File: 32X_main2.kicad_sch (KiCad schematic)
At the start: 43 parts, among them IC10 TC511664, IC509 74AC04, IC510 RHSRL33A, IC7 315-5818-B, IC8 315-5781, IC9 TC511664

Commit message: Start PCB layout.
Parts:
- removed IC7: 315-5818-B, symbol 32X:315-5818-B
- added IC504: 315-5818, Package_QFP:LQFP-176_24x24mm_P0.5mm, symbol 32X:315-5818
- C511, C512, C513, C514, C515, C516, C520, C521, C522, C523, C525, C526, C530, C531, C532, C533, C534, C535, C537, C538, C539, C540, C541, C596, C597, C599: footprint (none) -> Capacitor_SMD:C_0805_2012Metric
- IC501, IC502: value ~ -> SH2; footprint (none) -> Package_QFP:LQFP-144_20x20mm_P0.5mm
- IC503: value ~ -> uPD4502161; footprint (none) -> Package_SO:TSSOP-50_4.4x12.5mm_P0.5mm
- IC506: renamed from IC8; footprint (none) -> Package_QFP:LQFP-144_20x20mm_P0.5mm
- IC507: renamed from IC9; footprint (none) -> Package_SO:VSO-40_7.6x15.4mm_P0.762mm
- IC508: renamed from IC10; footprint (none) -> Package_SO:VSO-40_7.6x15.4mm_P0.762mm
- IC509: footprint (none) -> Package_SO:SO-14_3.9x8.65mm_P1.27mm
- R502, R503, R505, R506, R507, R508, R509: footprint (none) -> Resistor_SMD:R_0805_2012Metric
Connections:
- net GND: now also IC504.111 (GND), IC504.133 (GND), IC504.134 (GND), IC504.175 (GND), IC504.176 (GND), IC504.23 (GND), IC504.45 (GND), IC504.46 (GND), IC504.87 (GND), IC504.88 (GND)
- net SHA1: now also IC504.35 (SHA1)
- net SHA10: now also IC504.47 (SHA10)
- net SHA11: now also IC504.48 (SHA11)
- net SHA12: now also IC504.49 (SHA12)
- net SHA13: now also IC504.50 (SHA13)
- net SHA14: now also IC504.51 (SHA14)
- net SHA15: now also IC504.52 (SHA15)
- net SHA16: now also IC504.53 (SHA16)
- net SHA17: now also IC504.54 (SHA17)
- net SHA2: now also IC504.36 (SHA2)
- net SHA3: now also IC504.37 (SHA3)
- net SHA4: now also IC504.38 (SHA4)
- net SHA5: now also IC504.39 (SHA5)
- net SHA6: now also IC504.40 (SHA6)
- net SHA7: now also IC504.41 (SHA7)
- net SHA8: now also IC504.42 (SHA8)
- net SHA9: now also IC504.43 (SHA9)
- net SHD0: now also IC504.26 (SHD0)
- net SHD1: now also IC504.25 (SHD1)
- net SHD10: now also IC504.14 (SHD10)
- net SHD11: now also IC504.13 (SHD11)
- net SHD12: now also IC504.12 (SHD12)
- net SHD13: now also IC504.11 (SHD13)
- net SHD14: now also IC504.10 (SHD14)
- net SHD15: now also IC504.9 (SHD15)
- net SHD2: now also IC504.24 (SHD2)
- net SHD3: now also IC504.21 (SHD3)
- net SHD4: now also IC504.20 (SHD4)
- net SHD5: now also IC504.19 (SHD5)
- net SHD6: now also IC504.18 (SHD6)
- net SHD7: now also IC504.17 (SHD7)
- net SHD8: now also IC504.16 (SHD8)
- net SHD9: now also IC504.15 (SHD9)
- net SHDREQ0: now also IC504.66 (~{DREQ0})
- net SHDREQ1: now also IC504.65 (~{DREQ1})
- net SHRDWR: now also IC504.59 (RDWR)
- net VCC2: now also IC504.1 (VCC), IC504.110 (VCC), IC504.132 (VCC), IC504.22 (VCC), IC504.44 (VCC), IC504.89 (VCC)
- net ~{SHBS}: now also IC504.60 (~{BS})
- net ~{SHCS0M}: now also IC504.64 (~{CS0M})
- net ~{SHCS0S}: now also IC504.63 (~{CS0S})
- net ~{SHCS1}: now also IC504.62 (~{CS1})
- net ~{SHCS2}: now also IC504.61 (~{CS2})
- net ~{SHDQMLL}: now also IC504.57 (~{DQLL})
- net ~{SHDQMLU}: now also IC504.58 (~{DQLU})
- net ~{SHMIRL1}: now also IC504.30 (~{MIRL1})
- net ~{SHMIRL2}: now also IC504.31 (~{MIRL2})
- net ~{SHMIRL3}: now also IC504.32 (~{MIRL3})
- net ~{SHRD0}: now also IC504.56 (~{RD})
- net ~{SHRES}: now also IC504.34 (~{SHRES})
- net ~{SHSIRL1}: now also IC504.27 (~{SIRL1})
- net ~{SHSIRL2}: now also IC504.28 (~{SIRL2})
- net ~{SHSIRL3}: now also IC504.29 (~{SIRL3})
- net ~{SHWAIT}: now also IC504.55 (~{WAIT})
- net at C525.1, IC506.61 (ACCS): now also IC504.125 (ACCS)
- net at IC506.39 (AD15): now also IC504.150 (AD15)
- net at IC506.40 (AD14): now also IC504.149 (AD14)
- net at IC506.41 (AD13): now also IC504.148 (AD13)
- net at IC506.42 (AD12): now also IC504.147 (AD12)
- net at IC506.43 (AD11): now also IC504.146 (AD11)
- net at IC506.44 (AD10): now also IC504.145 (AD10)
- net at IC506.45 (AD9): now also IC504.144 (AD9)
- net at IC506.46 (AD8): now also IC504.143 (AD8)
- net at IC506.47 (AD7): now also IC504.142 (AD7)
- net at IC506.48 (AD6): now also IC504.141 (AD6)
- net at IC506.49 (AD5): now also IC504.140 (AD5)
- net at IC506.50 (AD4): now also IC504.139 (AD4)
- net at IC506.51 (AD3): now also IC504.138 (AD3)
- net at IC506.52 (AD2): now also IC504.137 (AD2)
- net at IC506.53 (AD1): now also IC504.136 (AD1)
- net at IC506.54 (AD0): now also IC504.135 (AD0)
- net at IC506.56 (C23): now also IC504.131 (C23)
- net at IC506.58 (RD): now also IC504.127 (RW)
- net at IC506.59 (DIR): now also IC504.126 (DIR)
- net at IC506.60 (VACK): now also IC504.124 (VACK)
- net at IC506.62 (HINT): now also IC504.122 (HINT)
- net at IC506.63 (VINT): now also IC504.123 (VINT)

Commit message: Save first mock-up before updating footprints.
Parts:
- added C517, C527: 4.7uF, Capacitor_SMD:C_0805_2012Metric, symbol Device:C
- added C518, C519, C528, C536: 100nF, Capacitor_SMD:C_0805_2012Metric, symbol Device:C
- IC503: footprint Package_SO:TSSOP-50_4.4x12.5mm_P0.5mm -> Neptune:SSOP-50
- IC507, IC508: footprint Package_SO:VSO-40_7.6x15.4mm_P0.762mm -> Neptune:SO-Mix-40
- L501: footprint (none) -> Inductor_SMD:L_0805_2012Metric
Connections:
- net VCC2: now also C537.1, C538.1, C539.1, C540.1, C541.1, C599.1, IC506.137 (DVDD), IC507.1 (VCC), IC507.11 (VCC), IC507.20 (VCC), IC508.1 (VCC), IC508.11 (VCC), IC508.20 (VCC), C517.1, C518.1, C519.1, C527.1, C528.1, C536.1
- net ~{SHCKE}: now also IC501.88 (~{CKE})
- net at C530.1, C531.1, IC506.115 (AVDD)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: no longer IC506.137 (DVDD)
- net GND renamed GND2
- net GND2: now also C517.2, C518.2, C519.2, C527.2, C528.2, C536.2
- net GNDA renamed GNDA2

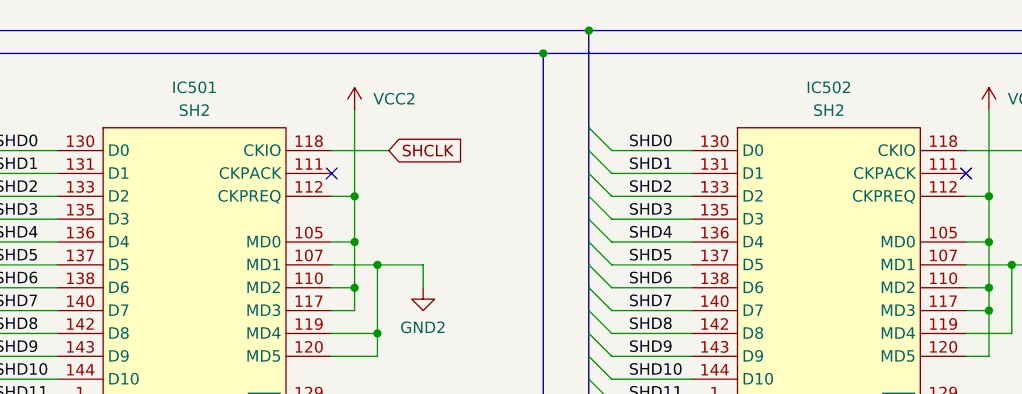
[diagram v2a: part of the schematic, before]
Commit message: Draft new layout with more accurate footprints.
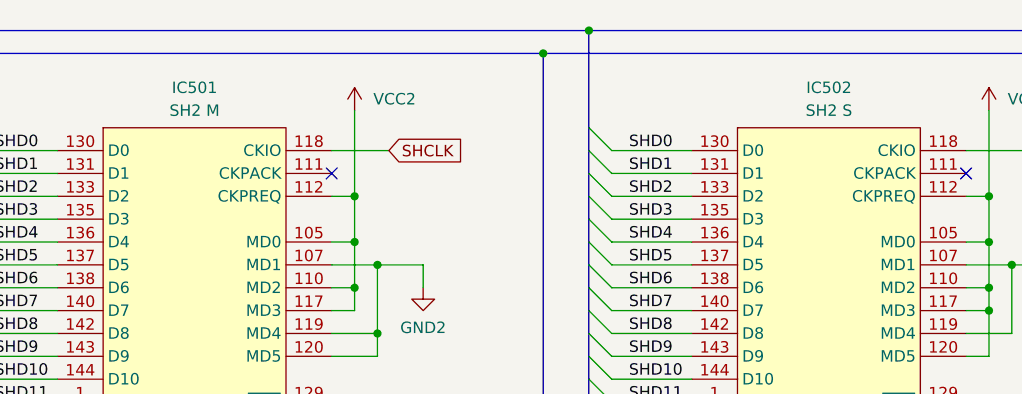
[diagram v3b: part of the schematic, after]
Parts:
- C512, C515, C517, C520, C523, C527, C530, C534, C537, C599: footprint Capacitor_SMD:C_0805_2012Metric -> Capacitor_SMD:C_1206_3216Metric
- IC501: value SH2 -> SH2 M
- IC502: value SH2 -> SH2 S
- IC510: footprint (none) -> Package_TO_SOT_SMD:SOT-89-3_Handsoldering
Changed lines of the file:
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@@
       (effects (font (size 1.27 1.27)) (justify right))
     )
-    (property "Footprint" "Capacitor_SMD:C_0805_2012Metric" (at 366.6998 59.055 0)
+    (property "Footprint" "Capacitor_SMD:C_1206_3216Metric" (at 366.6998 59.055 0)
       (effects (font (size 1.27 1.27)) hide)
     )
@@
       (effects (font (size 1.27 1.27)))
     )
-    (property "Value" "SH2" (at 48.895 25.4 0)
+    (property "Value" "SH2 M" (at 48.895 25.4 0)
       (effects (font (size 1.27 1.27)))
     )
@@
       (effects (font (size 1.27 1.27)))
     )
-    (property "Value" "SH2" (at 119.38 25.4 0)
+    (property "Value" "SH2 S" (at 119.38 25.4 0)
       (effects (font (size 1.27 1.27)))
     )
@@
       (effects (font (size 1.27 1.27)) (justify right))
     )
-    (property "Footprint" "Capacitor_SMD:C_0805_2012Metric" (at 366.6998 83.82 0)
+    (property "Footprint" "Capacitor_SMD:C_1206_3216Metric" (at 366.6998 83.82 0)
       (effects (font (size 1.27 1.27)) hide)
     )
@@
       (effects (font (size 1.27 1.27)) (justify right))
     )
-    (property "Footprint" "Capacitor_SMD:C_0805_2012Metric" (at 226.3902 79.375 0)
+    (property "Footprint" "Capacitor_SMD:C_1206_3216Metric" (at 226.3902 79.375 0)
       (effects (font (size 1.27 1.27)) hide)
     )
@@
       (effects (font (size 1.27 1.27)) (justify right))
     )
-    (property "Footprint" "Capacitor_SMD:C_0805_2012Metric" (at 296.8498 210.82 0)
+    (property "Footprint" "Capacitor_SMD:C_1206_3216Metric" (at 296.8498 210.82 0)
       (effects (font (size 1.27 1.27)) hide)
     )
@@
       (effects (font (size 1.27 1.27)) (justify right))
     )
-    (property "Footprint" "Capacitor_SMD:C_0805_2012Metric" (at 296.8498 116.205 0)
+    (property "Footprint" "Capacitor_SMD:C_1206_3216Metric" (at 296.8498 116.205 0)
       (effects (font (size 1.27 1.27)) hide)
     )
@@
       (effects (font (size 1.27 1.27)) (justify right))
     )
-    (property "Footprint" "Capacitor_SMD:C_0805_2012Metric" (at 152.7048 196.215 0)
+    (property "Footprint" "Capacitor_SMD:C_1206_3216Metric" (at 152.7048 196.215 0)
       (effects (font (size 1.27 1.27)) hide)
     )
@@
       (effects (font (size 1.27 1.27)) (justify right))
     )
-    (property "Footprint" "Capacitor_SMD:C_0805_2012Metric" (at 82.2198 196.215 0)
+    (property "Footprint" "Capacitor_SMD:C_1206_3216Metric" (at 82.2198 196.215 0)
       (effects (font (size 1.27 1.27)) hide)
     )
@@
       (effects (font (size 1.27 1.27)) (justify right))
     )
-    (property "Footprint" "Capacitor_SMD:C_0805_2012Metric" (at 171.1198 98.425 0)
+    (property "Footprint" "Capacitor_SMD:C_1206_3216Metric" (at 171.1198 98.425 0)
       (effects (font (size 1.27 1.27)) hide)
     )
@@
       (effects (font (size 1.27 1.27)) (justify right))
     )
-    (property "Footprint" "Capacitor_SMD:C_0805_2012Metric" (at 191.4398 121.92 0)
+    (property "Footprint" "Capacitor_SMD:C_1206_3216Metric" (at 191.4398 121.92 0)
       (effects (font (size 1.27 1.27)) hide)
     )
@@
       (effects (font (size 1.27 1.27)))
     )
-    (property "Footprint" "" (at 179.705 116.205 0)
+    (property "Footprint" "Package_TO_SOT_SMD:SOT-89-3_Handsoldering" (at 179.705 116.205 0)
       (effects (font (size 1.27 1.27) italic) (justify left) hide)
     )
@@
       (effects (font (size 1.27 1.27)) (justify right))
     )
-    (property "Footprint" "Capacitor_SMD:C_0805_2012Metric" (at 224.4852 257.81 0)
-      (effects (font (size 1.27 1.27)) hide)
-    )
+    (property "Footprint" "Capacitor_SMD:C_1206_3216Metric" (at 224.4852 257.81 0)
+      (effects (font (size 1.27 1.27)) hide)
+    )

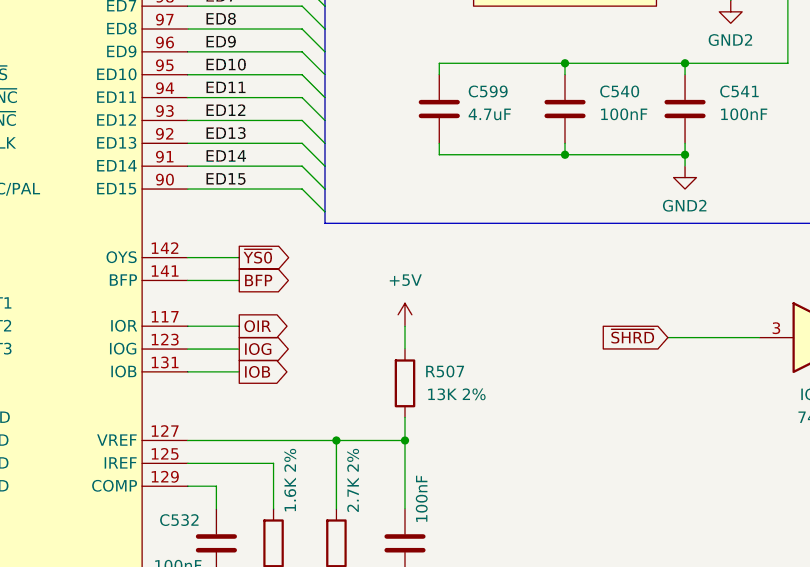
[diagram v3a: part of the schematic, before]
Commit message: Place remaining passives.
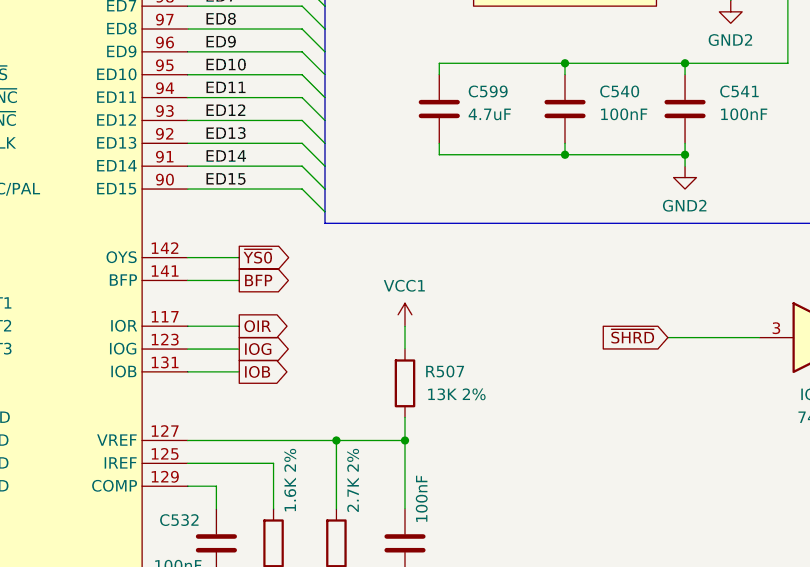
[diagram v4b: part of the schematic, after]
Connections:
- net +5V renamed VCC1
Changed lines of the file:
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@@
-    )
-  )
-  (symbol (lib_id "power:+5V") (at 294.005 231.14 0) (unit 1)
-    (in_bom yes) (on_board yes) (dnp no) (fields_autoplaced)
-    (property "Reference" "#PWR081" (at 294.005 234.95 0)
-      (effects (font (size 1.27 1.27)) hide)
-    )
-    (property "Value" "+5V" (at 294.005 226.06 0)
-      (effects (font (size 1.27 1.27)))
-    )
-    (property "Footprint" "" (at 294.005 231.14 0)
-      (effects (font (size 1.27 1.27)) hide)
-    )
-    (property "Datasheet" "" (at 294.005 231.14 0)
-      (effects (font (size 1.27 1.27)) hide)
-    )
-    (pin "1")
-    (instances
-      (project "Neptune"
-        (path "/bcc23b51-b742-4ae5-9dd6-d96a24058944/e4c57f96-d802-4292-9df6-7ff62ef14a9e"
-          (reference "#PWR081") (unit 1)
-        )
-      )
     )
   )
@@
         )
       )
+    )
+  )
+  (symbol (lib_id "MegaDrive:VCC1") (at 294.005 231.14 0) (unit 1)
+    (in_bom yes) (on_board yes) (dnp no) (fields_autoplaced)
+    (property "Reference" "#PWR0159" (at 294.005 234.95 0)
+      (effects (font (size 1.27 1.27)) hide)
+    )
+    (property "Value" "VCC1" (at 294.005 226.695 0)
+      (effects (font (size 1.27 1.27)))
+    )
+    (property "Footprint" "" (at 294.005 231.14 0)
+      (effects (font (size 1.27 1.27)) hide)
+    )
+    (property "Datasheet" "" (at 294.005 231.14 0)
+      (effects (font (size 1.27 1.27)) hide)
+    )
+    (pin "1")
+    (instances
+      (project "Neptune"
+        (path "/bcc23b51-b742-4ae5-9dd6-d96a24058944/01513199-62c5-4123-a151-ccd381a5e6c1"
+          (reference "#PWR0159") (unit 1)
+        )
+        (path "/bcc23b51-b742-4ae5-9dd6-d96a24058944/e4c57f96-d802-4292-9df6-7ff62ef14a9e"
+          (reference "#PWR081") (unit 1)
+        )
+      )

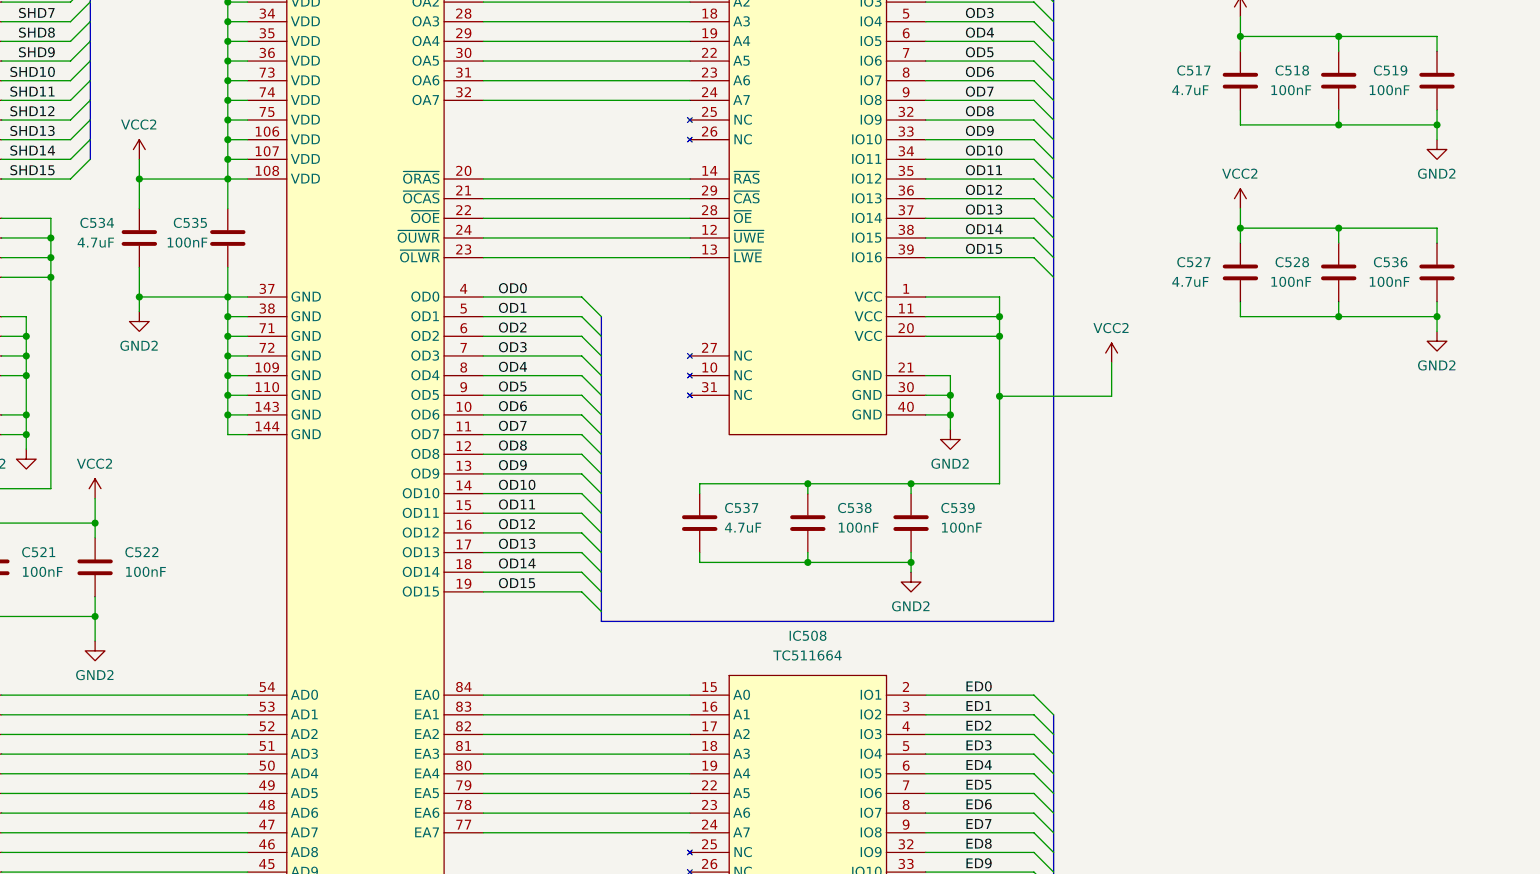
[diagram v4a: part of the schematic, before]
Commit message: Add missing/extra decoupling on 32X side.
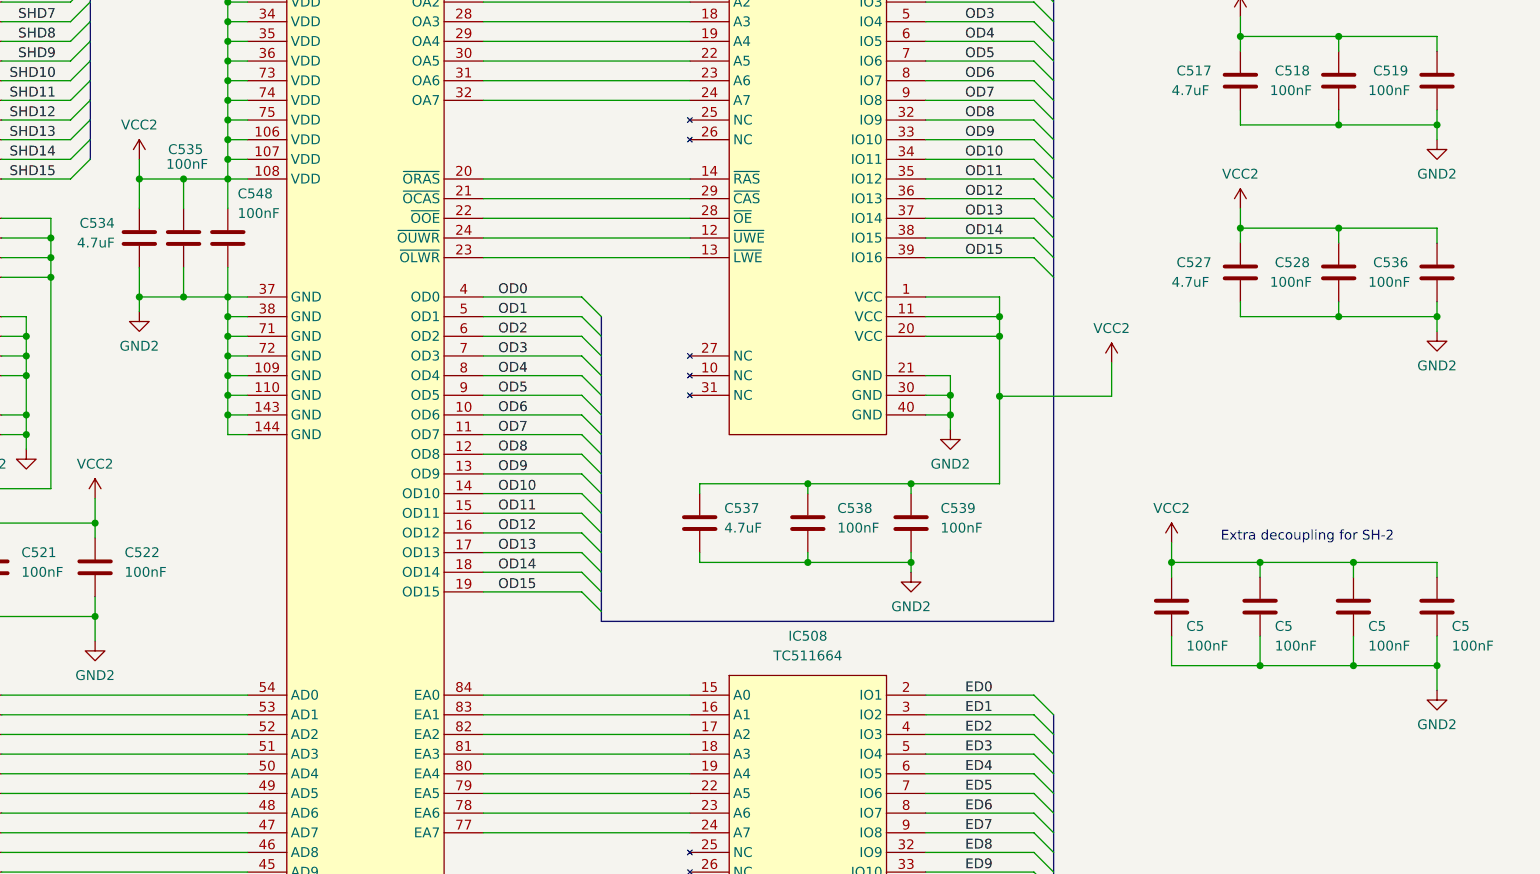
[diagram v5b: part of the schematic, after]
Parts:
- added C5 (x4), C548: 100nF, Capacitor_SMD:C_0805_2012Metric, symbol Device:C
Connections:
- net GND2: now also C5.2, C5.2, C5.2, C5.2, C548.2
- net VCC2: now also C5.1, C5.1, C5.1, C5.1, C548.1
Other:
- note added: "Extra decoupling for SH-2"
- moved on the sheet: C535
